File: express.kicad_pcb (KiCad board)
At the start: 4 copper layers, 180 x 35 mm, 180 parts, among them J1001 SJ2-25404B-SMT-TR, J101 Cortex_Debug, J102 JAE_DX07S016JA3, J1101 SJ2-25404B-SMT-TR, J1201 SJ2-25404B-SMT-TR, J1301 SJ2-25404B-SMT-TR, J1401 SJ2-25404B-SMT-TR, J1501 SJ2-25404B-SMT-TR, J1601 SJ2-25404B-SMT-TR, J1701 SJ2-25404B-SMT-TR, J1801 SJ2-25404B-SMT-TR, J201 SJ2-25404B-SMT-TR, J301 SJ2-25404B-SMT-TR, J401 SJ2-25404B-SMT-TR, J501 SJ2-25404B-SMT-TR, J601 SJ2-25404B-SMT-TR, J701 SJ2-25404B-SMT-TR, J801 SJ2-25404B-SMT-TR, J901 SJ2-25404B-SMT-TR, SW101 SW_Push, SW102 SW_Push, U101 TPS78433QWDRBRQ1, U103 ATSAMD51J, U201 74AHC1G125, Y102 32k768

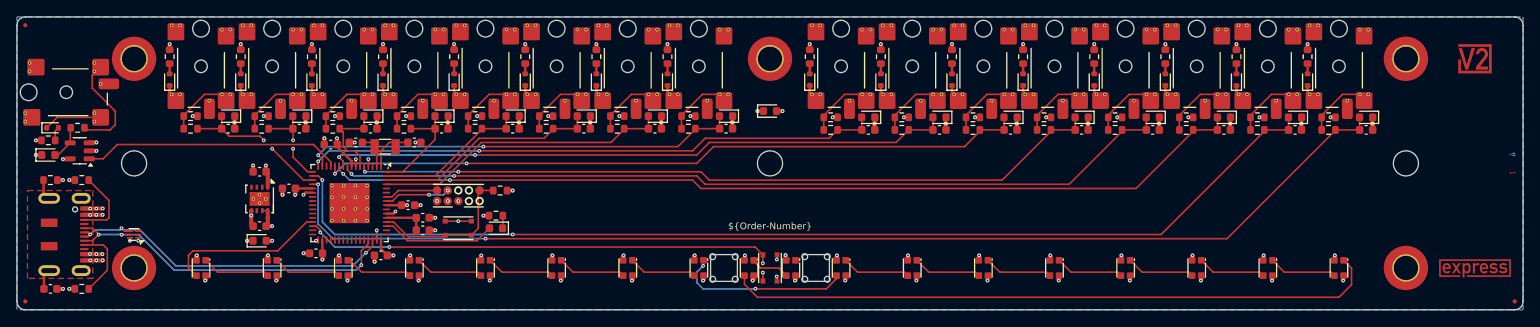
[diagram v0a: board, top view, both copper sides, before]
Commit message: Convert to V2 Link
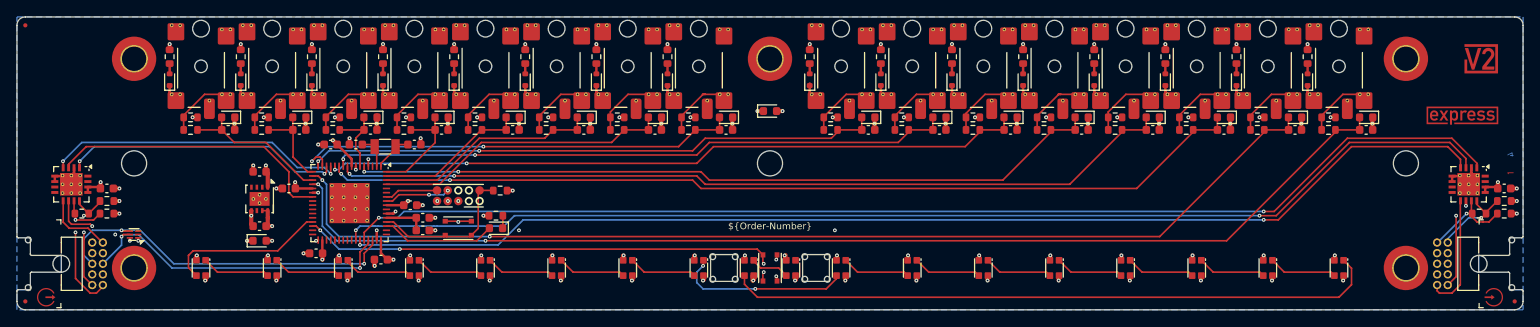
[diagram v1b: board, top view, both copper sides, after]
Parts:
- removed the C101 at (66.5, 117.2)
- removed the D201 at (66.8, 98.0)
- removed J102: JAE_DX07S016JA3, V2_Connector_USB:JAE_DX07S016JA3
- removed the J201 at (68.0, 93.8)
- removed the R101 at (66.5, 104.2)
- removed R103, R104: 5k1, Resistor_SMD:R_0603_1608Metric
- removed the R201 at (69.8, 98.0)
- removed the R202 at (66.2, 99.5)
- removed the TVS201 at (66.2, 101.2)
- removed U201: 74AHC1G125, Package_TO_SOT_SMD:SOT-23-5
- added C1801: 0u1, Capacitor_SMD:C_0603_1608Metric, F.Cu at (73.2, 105.2)
- added C1901: 0u1, Capacitor_SMD:C_0603_1608Metric, F.Cu at (240.2, 105.2)
- added ICON101: Arrow_In, V2_Artwork:Arrow_In, F.Cu at (239.0, 118.2)
- added ICON102: Arrow_Out, V2_Artwork:Arrow_Out, F.Cu at (66.0, 118.2)
- added J1801: 2x05_Horizontal, V2_Connector_Header_1.27mm:PinHeader_2x05_P1.27mm_Horizontal, F.Cu at (71.5, 114.2)
- added J1901: 2x05_Horizontal, V2_Connector_Header_1.27mm:PinHeader_2x05_P1.27mm_Horizontal, F.Cu at (233.5, 114.2)
- added PLUG101: PCB_Plug_Horizontal, V2_PCB_Devices:PCB_Plug_Horizontal, F.Cu at (71.5, 114.2)
- added PLUG102: PCB_Plug_Horizontal, V2_PCB_Devices:PCB_Plug_Horizontal, F.Cu at (233.5, 114.2)
- added R1801: 10k, Resistor_SMD:R_0603_1608Metric, F.Cu at (73.2, 106.8)
- added R1802: 120R, Resistor_SMD:R_0603_1608Metric, F.Cu at (70.2, 108.2)
- added R1803: 10k, Resistor_SMD:R_0603_1608Metric, F.Cu at (73.2, 108.2)
- added R1901: 10k, Resistor_SMD:R_0603_1608Metric, F.Cu at (240.2, 106.8)
- added R1902: 120R, Resistor_SMD:R_0603_1608Metric, F.Cu at (237.2, 108.2)
- added R1903: 10k, Resistor_SMD:R_0603_1608Metric, F.Cu at (240.2, 108.2)
- added U1801: SN65MLVD203B, V2_Package_DFN_QFN:WQFN-16-1EP_4x4mm_P0.65mm_EP2.7x2.7mm_ThermalVias, F.Cu at (69.0, 104.8)
- added U1901: SN65MLVD203B, V2_Package_DFN_QFN:WQFN-16-1EP_4x4mm_P0.65mm_EP2.7x2.7mm_ThermalVias, F.Cu at (236.0, 104.8)
- moved ICON104 18.3 mm to (235.2, 96.5)
- moved ICON103 0.75 mm to (237.5, 89.8)
- moved C104 0.50 mm to (106.0, 113.8)
- moved C106 0.25 mm to (109.5, 107.2)
- moved C110 0.25 mm to (110.0, 100.0)
- moved C111 0.25 mm to (103.0, 100.0)
- moved INFO102 0.25 mm to (241.0, 102.2)
- moved C201 0.14 mm to (87.8, 98.2)
- moved C301 0.14 mm to (96.2, 98.2)
- moved C401 0.14 mm to (104.8, 98.2)
- moved C501 0.14 mm to (113.2, 98.2)
- moved C601 0.14 mm to (121.8, 98.2)
- moved C701 0.14 mm to (130.2, 98.2)
- moved C801 0.14 mm to (138.8, 98.2)
- moved C901 0.14 mm to (147.2, 98.2)
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- renumbered C1101 to C1001, C114 to C101, C115 to C102, C116 to C103, C117 to C104, C118 to C105, C119 to C106, C120 to C107, C110 to C108, C121 to C109, C112 to C110, C1201 to C1101, C113 to C111, C1301 to C1201, C1401 to C1301, C1501 to C1401, C1601 to C1501, C1701 to C1601, C1801 to C1701, C301 to C201, C401 to C301, C501 to C401, C601 to C501, C701 to C601, C801 to C701, C901 to C801, C1001 to C901, D1101 to D1001, D1102 to D1002, D102 to D101, D103 to D102, D101 to D103, D1201 to D1101, D1202 to D1102, D1301 to D1201, D1302 to D1202, D1401 to D1301, D1402 to D1302, D1501 to D1401, D1502 to D1402, D1601 to D1501, D1602 to D1502, D1701 to D1601, D1702 to D1602, D1801 to D1701, D1802 to D1702, D302 to D201, D301 to D202, D402 to D301, D401 to D302, D502 to D401, D501 to D402, D602 to D501, D601 to D502, D702 to D601, D701 to D602, D802 to D701, D801 to D702, D902 to D801, D901 to D802, D1002 to D901, D1001 to D902, ICON101 to ICON103, ICON102 to ICON104, J1101 to J1001, J1201 to J1101, J1301 to J1201, J1401 to J1301, J1501 to J1401, J1601 to J1501, J1701 to J1601, J1801 to J1701, J301 to J201, J401 to J301, J501 to J401, J601 to J501, J701 to J601, J801 to J701, J901 to J801, J1001 to J901, R1101 to R1001, R1103 to R1002, R1102 to R1003, R102 to R101, R105 to R102, R1201 to R1101, R1203 to R1102, R1202 to R1103, R1301 to R1201, R1303 to R1202, R1302 to R1203, R1401 to R1301, R1403 to R1302, R1402 to R1303, R1501 to R1401, R1503 to R1402, R1502 to R1403, R1601 to R1501, R1603 to R1502, R1602 to R1503, R1701 to R1601, R1703 to R1602, R1702 to R1603, R1801 to R1701, R1803 to R1702, R1802 to R1703, R301 to R201, R302 to R202, R303 to R203, R401 to R301, R402 to R302, R403 to R303, R501 to R401, R502 to R402, R503 to R403, R601 to R501, R602 to R502, R603 to R503, R701 to R601, R702 to R602, R703 to R603, R801 to R701, R802 to R702, R803 to R703, R901 to R801, R902 to R802, R903 to R803, R1001 to R901, R1002 to R902, R1003 to R903, SW102 to SW101, SW101 to SW102, TVS1101 to TVS1001, TVS102 to TVS101, TVS101 to TVS102, TVS1201 to TVS1101, TVS1301 to TVS1201, TVS1401 to TVS1301, TVS1501 to TVS1401, TVS1601 to TVS1501, TVS1701 to TVS1601, TVS1801 to TVS1701, TVS301 to TVS201, TVS401 to TVS301, TVS501 to TVS401, TVS601 to TVS501, TVS701 to TVS601, TVS801 to TVS701, TVS901 to TVS801, TVS1001 to TVS901, U103 to U102, Y102 to Y101
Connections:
- SPACER101 pad 1: Earth -> GND
- SPACER102 pad 1: Earth -> GND
- SPACER103 pad 1: Earth -> GND
- SPACER104 pad 1: Earth -> GND
- SPACER105 pad 1: Earth -> GND
- U102 pad 13: /MIDI-Out -> /Plug-TX
- U102 pad 14: unconnected-(U103-PA05-Pad14) -> /Plug-RX
- U102 pad 23: unconnected-(U103-PB10-Pad23) -> /Plug-TX-Enable
- U102 pad 42: unconnected-(U103-PA21-Pad42) -> /Socket-TX-Enable
- U102 pad 43: unconnected-(U103-PA22-Pad43) -> /Socket-TX
- U102 pad 44: unconnected-(U103-PA23-Pad44) -> /Socket-RX
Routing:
- net /Socket-RX: track 0.00 -> 140.3 mm, vias 0 -> 2
- net /Socket-TX-Enable: track 0.00 -> 140.1 mm, vias 0 -> 2
- net /Socket-TX: track 0.00 -> 138.6 mm, vias 0 -> 2
- net /Plug-TX: track 0.00 -> 36.2 mm, vias 0 -> 2
- net /Plug-TX-Enable: track 0.00 -> 34.4 mm
- net /Plug-RX: track 0.00 -> 33.1 mm, vias 0 -> 2
- net /MIDI-Out: track 30.9 -> 0.00 mm
- net /Link Plug/RX-B: track 0.00 -> 17.1 mm, vias 0 -> 2
- net /Link Socket/TX-Y: track 0.00 -> 14.0 mm
- net /Link Plug/RX-A: track 0.00 -> 13.5 mm, vias 0 -> 2
- net /MIDI Out/Tip: track 12.5 -> 0.00 mm
- net /Link Socket/RX-B: track 0.00 -> 11.3 mm, vias 0 -> 1
- net /Link Socket/TX-Z: track 0.00 -> 11.0 mm, vias 0 -> 2
- net /Link Socket/RX-A: track 0.00 -> 10.3 mm, vias 0 -> 1
- net /USB-CC2: track 8.64 -> 0.00 mm
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- added copper zone on B.Cu, net GND
- removed copper zone on B.Cu, net Earth
- removed copper zone on F.Cu, net Earth
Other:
- outline, holes or cut-outs redrawn

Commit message: Update
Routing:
- net GND: vias 82 -> 83
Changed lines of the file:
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@@
 	)
 	(via
+		(at 100.5 101.25)
+		(size 0.45)
+		(drill 0.2)
+		(layers "F.Cu" "B.Cu")
+		(remove_unused_layers yes)
+		(keep_end_layers yes)
+		(free yes)
+		(zone_layer_connections "In1.Cu")
+		(net 1)
+	)
+	(via
 		(at 154.25 113.25)
 		(size 0.45)
@@
 		(net 1)
 		(net_name "GND")
-		(layer "B.Cu")
-		(hatch edge 0.508)
-		(connect_pads
-			(clearance 0.2)
-		)
-		(min_thickness 0.25)
-		(filled_areas_thickness no)
-		(fill yes
-			(thermal_gap 0.508)
-			(thermal_bridge_width 0.508)
-			(smoothing fillet)
-			(radius 0.2)
-		)
-		(polygon
-			(pts
-				(xy 242.5 119.75) (xy 62.5 119.75) (xy 62.5 84.75) (xy 242.5 84.75)
-			)
-		)
-	)
-	(zone
-		(net 1)
-		(net_name "GND")
-		(layer "In1.Cu")
+		(layers "B.Cu" "In1.Cu")
 		(hatch edge 0.508)
 		(connect_pads yes

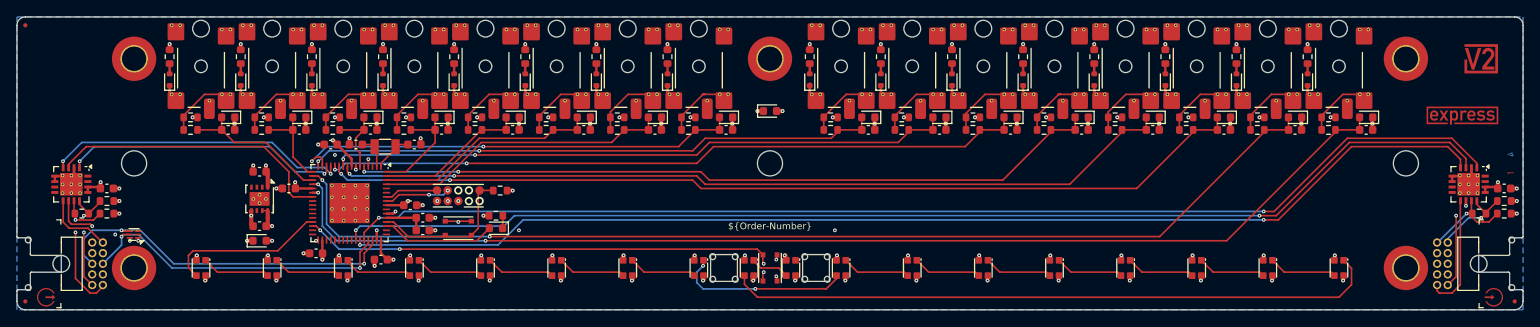
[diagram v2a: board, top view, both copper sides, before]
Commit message: Move transceiver
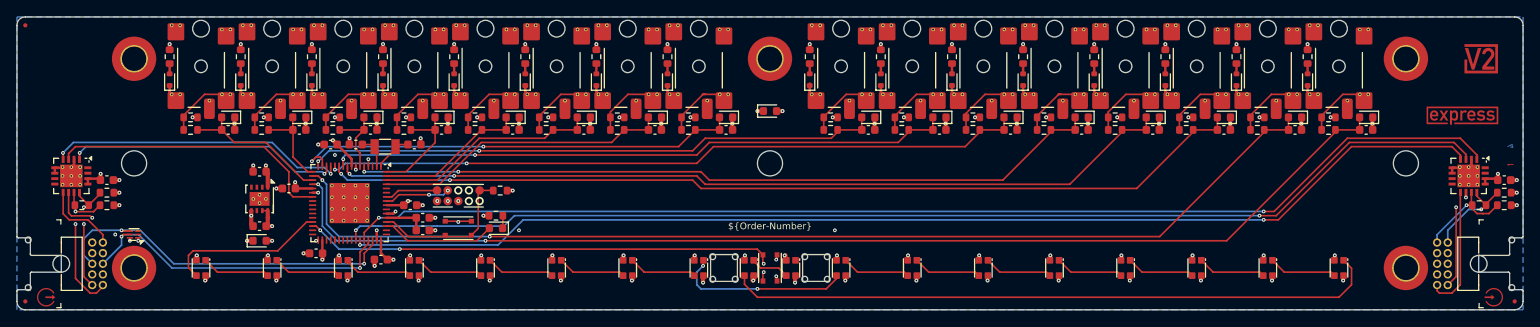
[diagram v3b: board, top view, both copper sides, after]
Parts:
- moved C1801 1.00 mm to (73.2, 104.2)
- moved C1901 1.00 mm to (240.2, 104.2)
- moved INFO102 1.00 mm to (241.0, 101.2)
- moved R1801 1.00 mm to (73.2, 105.8)
- moved R1802 1.00 mm to (70.2, 107.2)
- moved R1803 1.00 mm to (73.2, 107.2)
- moved R1901 1.00 mm to (240.2, 105.8)
- moved R1902 1.00 mm to (237.2, 107.2)
- moved R1903 1.00 mm to (240.2, 107.2)
- moved U1801 1.00 mm to (69.0, 103.8)
- moved U1901 1.00 mm to (236.0, 103.8)
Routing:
- net /Link Socket/RX-B: track 11.3 -> 12.3 mm
- net /Link Plug/RX-B: track 17.1 -> 18.1 mm
- net /Link Socket/TX-Z: track 11.0 -> 12.0 mm
- net /Link Socket/TX-Y: track 14.0 -> 15.0 mm
- net /Link Socket/RX-A: track 10.3 -> 11.3 mm
- net /Link Plug/TX-Z: track 7.47 -> 8.47 mm
- net /Link Plug/RX-A: track 13.5 -> 14.5 mm
- net /Link Plug/TX-Y: track 8.30 -> 9.27 mm
- net /Socket-TX-Enable: track 140.1 -> 139.3 mm
- net /Socket-TX: track 138.6 -> 137.9 mm

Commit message: Update tranceiver
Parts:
- removed the R1801 at (73.2, 105.8)
- removed R1803, R1903: 10k, Resistor_SMD:R_0603_1608Metric
- removed the R1901 at (240.2, 105.8)
- U1801, U1901: value SN65MLVD203B -> THVD24x2; footprint V2_Package_DFN_QFN:WQFN-16-1EP_4x4mm_P0.65mm_EP2.7x2.7mm_ThermalVias -> V2_Package_SON:VSON-10-4-1EP_3x3mm_P0.5mm_EP1.65x2.4mm_ThermalVias
- moved C1901 2.30 mm to (238.0, 103.8), turned to 90 degrees
- moved R1901 2.00 mm to (235.2, 107.2)
- moved H101 1.00 mm to (77.5, 102.2)
- moved H102 1.00 mm to (227.5, 102.2)
- moved SPACER101 1.00 mm to (227.5, 89.8)
- moved SPACER102 1.00 mm to (77.5, 89.8)
- moved SPACER103 1.00 mm to (77.5, 114.8)
- moved SPACER104 1.00 mm to (227.5, 114.8)
- moved U1801 1.00 mm to (70.0, 103.8)
- moved U1901 1.00 mm to (235.0, 103.8)
- moved C1801 0.56 mm to (73.0, 103.8), turned to 90 degrees
- moved C108 0.25 mm to (91.5, 109.5)
- moved INFO102 0.25 mm to (241.2, 101.2)
- moved TVS101 0.25 mm to (91.5, 111.2)
- renumbered R1802 to R1801, R1902 to R1901
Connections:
- U1801 pad 10: /Link Plug/TX-Z -> +3V3
- U1801 pad 11: /Link Plug/RX-B -> GND
- U1801 pad 6: GND -> /Link Plug/TX-Y
- U1801 pad 7: unconnected-(U1801-Pad7) -> /Link Plug/TX-Z
- U1801 pad 8: unconnected-(U1801-Pad8) -> /Link Plug/RX-B
- U1801 pad 9: /Link Plug/TX-Y -> /Link Plug/RX-A
- U1901 pad 10: /Link Socket/TX-Z -> +3V3
- U1901 pad 11: /Link Socket/RX-B -> GND
- U1901 pad 6: GND -> /Link Socket/TX-Y
- U1901 pad 7: unconnected-(U1901-Pad7) -> /Link Socket/TX-Z
- U1901 pad 8: unconnected-(U1901-Pad8) -> /Link Socket/RX-B
- U1901 pad 9: /Link Socket/TX-Y -> /Link Socket/RX-A
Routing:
- net +5V: track 16.4 -> 11.8 mm
- net /Link Socket/RX-B: track 12.3 -> 8.38 mm, vias 1 -> 0
- net /Link Socket/RX-A: track 11.3 -> 7.83 mm, vias 1 -> 0
- net +3V3: track 38.4 -> 35.2 mm, vias 30 -> 29
- net GND: track 72.4 -> 69.7 mm, vias 83 -> 89
- net /Link Plug/RX-B: track 18.1 -> 15.7 mm, vias 2 -> 0
- net /Link Plug/RX-A: track 14.5 -> 12.6 mm, vias 2 -> 0
- net /Link Socket/TX-Y: track 15.0 -> 16.6 mm, vias 0 -> 2
- net /Plug-TX: track 35.8 -> 34.5 mm
- net /Link Plug/TX-Y: track 9.27 -> 10.5 mm, vias 0 -> 1
- net /Link Socket/TX-Z: track 12.0 -> 13.2 mm
- net /Plug-TX-Enable: track 34.2 -> 33.1 mm
- net /Socket-RX: track 139.9 -> 139.1 mm
- net /Plug-RX: track 32.7 -> 31.9 mm
- net /Link Plug/TX-Z: track 8.47 -> 8.98 mm
- added copper zone on F.Cu, net +3V3
- added copper zone on F.Cu, net +5V
- added copper zone on F.Cu, net GND
- added copper zone on In2.Cu, net GND

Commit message: Link termination
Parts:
- R1801, R1901: value 120R -> 100R

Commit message: Colours
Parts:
- removed C102: 0u1, Capacitor_SMD:C_0603_1608Metric
- H103: renamed from SPACER101; value 9774030243 -> MountingHole_2mm; footprint V2_Spacer_Wurth:9774030243 -> V2_Mechanical:MountingHole_2mm
- H104: renamed from SPACER102; value 9774030243 -> MountingHole_2mm; footprint V2_Spacer_Wurth:9774030243 -> V2_Mechanical:MountingHole_2mm
- H106: renamed from SPACER103; value 9774030243 -> MountingHole_2mm; footprint V2_Spacer_Wurth:9774030243 -> V2_Mechanical:MountingHole_2mm
- H107: renamed from SPACER104; value 9774030243 -> MountingHole_2mm; footprint V2_Spacer_Wurth:9774030243 -> V2_Mechanical:MountingHole_2mm
- H108: renamed from SPACER105; value 9774030243 -> MountingHole_2mm; footprint V2_Spacer_Wurth:9774030243 -> V2_Mechanical:MountingHole_2mm
- moved C101 1.80 mm to (109.5, 109.2)
- moved C105 0.75 mm to (95.8, 105.2), turned to -90 degrees
- renumbered H103 to H105
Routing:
- net GND: track 69.7 -> 85.5 mm, vias 89 -> 88
- net /VDDCORE: track 5.06 -> 2.27 mm
- net /Plug-TX-Enable: track 33.1 -> 34.4 mm
